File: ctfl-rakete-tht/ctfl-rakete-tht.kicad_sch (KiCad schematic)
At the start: 31 parts, among them J1 Conn_02x03_Odd_Even, SW1 SW_SPDT, U1 ATtiny212-SS

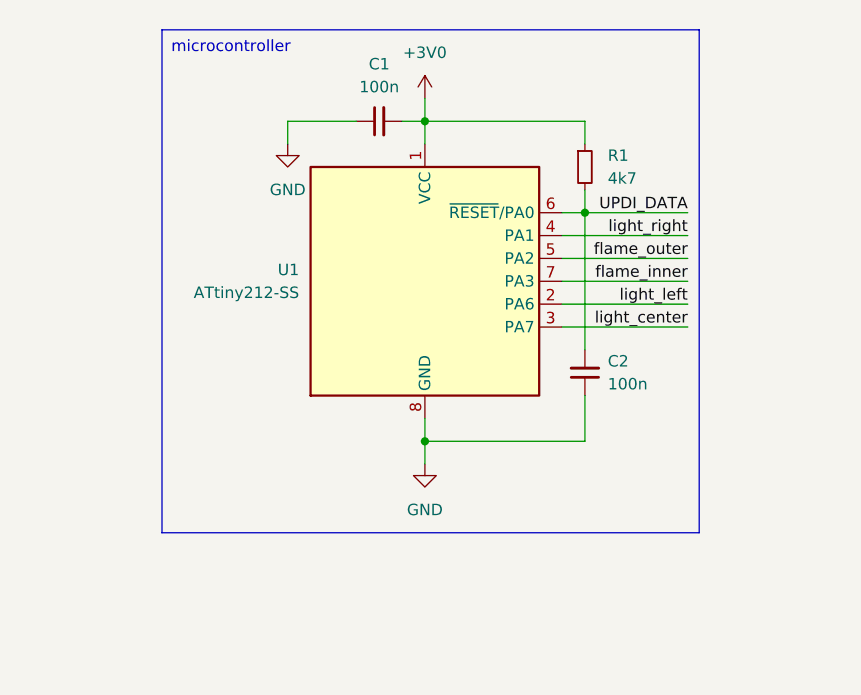
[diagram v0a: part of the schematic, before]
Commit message: added a second decoupling capacitor with 1 uF to the Controller supply
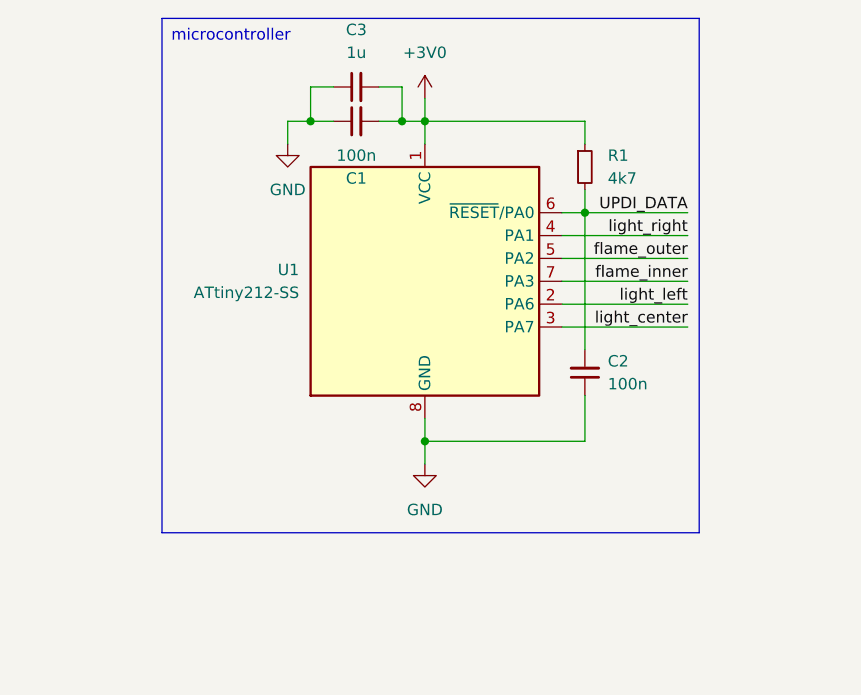
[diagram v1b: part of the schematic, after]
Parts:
- added C3: 1u, Capacitor_SMD:C_0805_2012Metric_Pad1.18x1.45mm_HandSolder, symbol Device:C_Small
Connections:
- net +3V0: now also C3.2
- net GND: now also C3.1
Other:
- moved on the sheet: C1
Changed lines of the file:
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@@
 	)
 	(junction
+		(at 127 30.48)
+		(diameter 0)
+		(color 0 0 0 0)
+	)
+	(junction
 		(at 195.58 128.27)
 		(diameter 0)
@@
 	)
 	(junction
+		(at 137.16 30.48)
+		(diameter 0)
+		(color 0 0 0 0)
+	)
+	(junction
 		(at 236.22 128.27)
 		(diameter 0)
@@
 	(wire
 		(pts
+			(xy 127 26.67) (xy 127 30.48)
+		)
+		(stroke
+			(width 0)
+			(type default)
+		)
+	)
+	(wire
+		(pts
 			(xy 157.48 38.1) (xy 157.48 40.64)
 		)
@@
 	(wire
 		(pts
+			(xy 137.16 26.67) (xy 137.16 30.48)
+		)
+		(stroke
+			(width 0)
+			(type default)
+		)
+	)
+	(wire
+		(pts
 			(xy 243.84 41.91) (xy 250.19 41.91)
 		)
@@
 	(wire
 		(pts
-			(xy 137.16 30.48) (xy 139.7 30.48)
+			(xy 134.62 30.48) (xy 137.16 30.48)
 		)
 		(stroke
@@
 	(wire
 		(pts
+			(xy 134.62 26.67) (xy 137.16 26.67)
+		)
+		(stroke
+			(width 0)
+			(type default)
+		)
+	)
+	(wire
+		(pts
 			(xy 129.54 129.54) (xy 129.54 130.81)
 		)
@@
 	(wire
 		(pts
+			(xy 127 30.48) (xy 129.54 30.48)
+		)
+		(stroke
+			(width 0)
+			(type default)
+		)
+	)
+	(wire
+		(pts
 			(xy 139.7 135.89) (xy 139.7 138.43)
 		)
@@
 	(wire
 		(pts
-			(xy 124.46 30.48) (xy 132.08 30.48)
+			(xy 124.46 30.48) (xy 127 30.48)
 		)
 		(stroke
@@
 	(wire
 		(pts
+			(xy 129.54 26.67) (xy 127 26.67)
+		)
+		(stroke
+			(width 0)
+			(type default)
+		)
+	)
+	(wire
+		(pts
 			(xy 236.22 128.27) (xy 246.38 128.27)
 		)
@@
 	(wire
 		(pts
+			(xy 137.16 30.48) (xy 139.7 30.48)
+		)
+		(stroke
+			(width 0)
+			(type default)
+		)
+	)
+	(wire
+		(pts
 			(xy 226.06 130.81) (xy 226.06 128.27)
 		)
@@
 	(text_box "microcontroller"
 		(exclude_from_sim no)
-		(at 110.49 20.32 0)
-		(size 59.69 55.88)
+		(at 110.49 19.05 0)
+		(size 59.69 57.15)
 		(stroke
 			(width 0)
@@
 	)
 	(symbol
+		(lib_id "Device:C_Small")
+		(at 132.08 26.67 90)
+		(unit 1)
+		(exclude_from_sim no)
+		(in_bom yes)
+		(on_board yes)
+		(dnp no)
+		(property "Reference" "C3"
+			(at 132.0863 20.32 90)
+			(effects
+				(font
+					(size 1.27 1.27)
+				)
+			)
+		)
+		(property "Value" "1u"
+			(at 132.0863 22.86 90)
+			(effects
+				(font
+					(size 1.27 1.27)
+				)
+			)
+		)
+		(property "Footprint" "Capacitor_SMD:C_0805_2012Metric_Pad1.18x1.45mm_HandSolder"
+			(at 132.08 26.67 0)
+			(effects
+				(font
+					(size 1.27 1.27)
+				)
+				(hide yes)
+			)
+		)
+		(property "Datasheet" "~"
+			(at 132.08 26.67 0)
+			(effects
+				(font
+					(size 1.27 1.27)
+				)
+				(hide yes)
+			)
+		)
+		(property "Description" "Unpolarized capacitor, small symbol"
+			(at 132.08 26.67 0)
+			(effects
+				(font
+					(size 1.27 1.27)
+				)
+				(hide yes)
+			)
+		)
+		(pin "1"
+		)
+		(pin "2"
+		)
+		(instances
+			(project "ctfl-rakete-tht"
+				(path "/829bb9b1-d184-4115-9887-268f3090b165"
+					(reference "C3")
+					(unit 1)
+				)
+			)
+		)
+	)
+	(symbol
 		(lib_id "Mechanical:MountingHole_Pad")
 		(at 40.64 175.26 270)
@@
 	(symbol
 		(lib_id "Device:C_Small")
-		(at 134.62 30.48 90)
+		(at 132.08 30.48 90)
+		(mirror x)
 		(unit 1)
 		(exclude_from_sim no)
@@
 		(on_board yes)
 		(dnp no)
-		(fields_autoplaced yes)
 		(property "Reference" "C1"
-			(at 134.6263 24.13 90)
+			(at 132.0863 36.83 90)
 			(effects
 				(font
@@
 		)
 		(property "Value" "100n"
-			(at 134.6263 26.67 90)
+			(at 132.0863 34.29 90)
 			(effects
 				(font
@@
 		)
 		(property "Footprint" "Capacitor_SMD:C_0805_2012Metric_Pad1.18x1.45mm_HandSolder"
-			(at 134.62 30.48 0)
+			(at 132.08 30.48 0)
 			(effects
 				(font
@@
 		)
 		(property "Datasheet" "~"
-			(at 134.62 30.48 0)
+			(at 132.08 30.48 0)
 			(effects
 				(font
@@
 		)
 		(property "Description" "Unpolarized capacitor, small symbol"
-			(at 134.62 30.48 0)
+			(at 132.08 30.48 0)
 			(effects
 				(font
